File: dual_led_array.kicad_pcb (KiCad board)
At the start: 2 copper layers, 254 x 254 mm, 187 parts, among them J1 Screw_Terminal_01x02, J2 Screw_Terminal_01x02, M1 quarter_twenty, M2 quarter_twenty, M3 quarter_twenty, M4 quarter_twenty

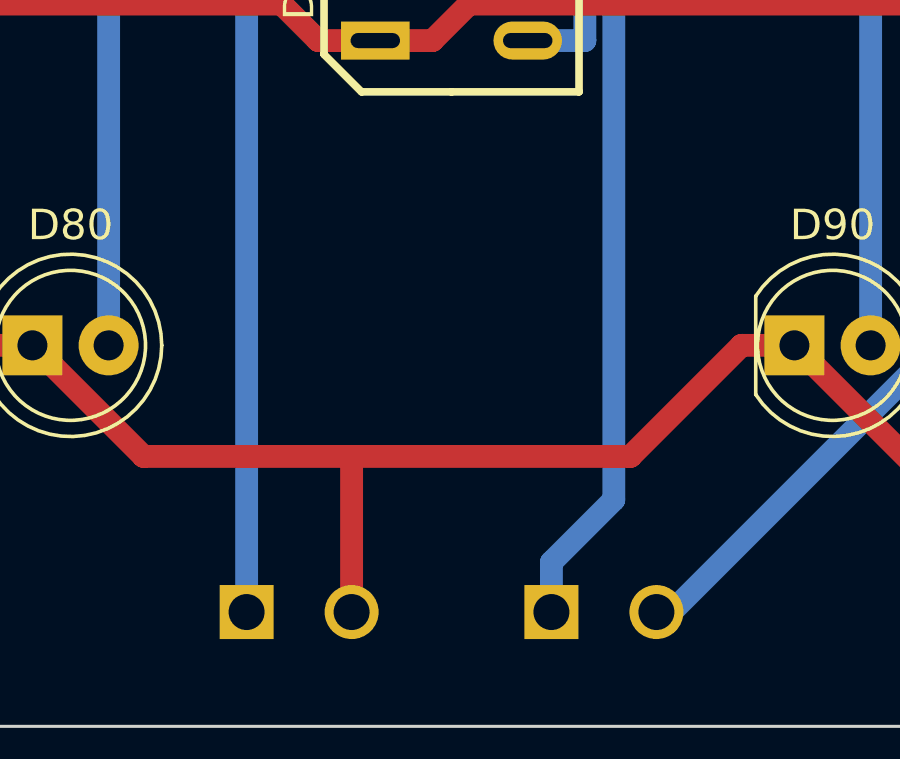
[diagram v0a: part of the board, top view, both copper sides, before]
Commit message: Added annotations to PCB.
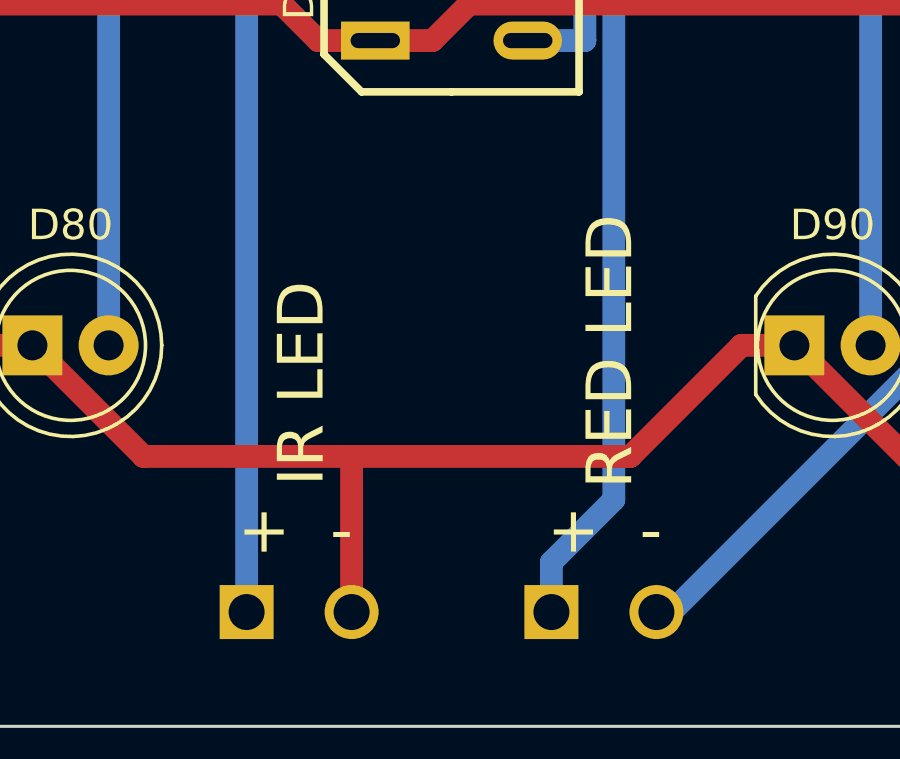
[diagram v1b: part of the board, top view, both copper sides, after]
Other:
- board text added: "+ -"
- board text added: "- +"
- board text added: "Dual LED Array V0.1 Dickinson Lab 2019"
- board text added: "IR LED"
- board text added: "RED LED"
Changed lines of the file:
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@@
   (general
     (thickness 1.6)
-    (drawings 10)
+    (drawings 21)
     (tracks 1220)
     (zones 0)
@@
     (descr BLOCK_CONN_2X1)
     (tags BLOCK_CONN_2X1)
-    (fp_text reference J1 (at -5.08 2.54) (layer B.SilkS)
+    (fp_text reference J1 (at -5.334 -2.7432) (layer B.SilkS)
       (effects (font (size 1.016 1.016) (thickness 0.2032)) (justify mirror))
     )
@@
     (descr BLOCK_CONN_2X1)
     (tags BLOCK_CONN_2X1)
-    (fp_text reference J2 (at -5.08 2.54) (layer B.SilkS)
+    (fp_text reference J2 (at 5.334 -2.8702) (layer B.SilkS)
       (effects (font (size 1.016 1.016) (thickness 0.2032)) (justify mirror))
     )
@@
       (net 94 "Net-(D101-Pad2)"))
   )
+  (gr_text "Dual LED Array V0.1\nDickinson Lab 2019" (at 177.8 300.5074) (layer B.SilkS)
+    (effects (font (size 1.524 1.524) (thickness 0.3048)) (justify mirror))
+  )
+  (gr_text "-  +" (at 259.1308 295.8338) (layer B.SilkS)
+    (effects (font (size 1.524 1.524) (thickness 0.3048)) (justify mirror))
+  )
+  (gr_text "-  +" (at 248.6914 295.8338) (layer B.SilkS)
+    (effects (font (size 1.524 1.524) (thickness 0.3048)) (justify mirror))
+  )
+  (gr_text "RED LED" (at 259.2324 290.4744 90) (layer B.SilkS)
+    (effects (font (size 1.524 1.524) (thickness 0.3048)) (justify mirror))
+  )
+  (gr_text "IR LED" (at 248.9454 291.2618 90) (layer B.SilkS)
+    (effects (font (size 1.524 1.524) (thickness 0.3048)) (justify mirror))
+  )
+  (gr_text "+  -" (at 259.1054 298.2722) (layer F.SilkS)
+    (effects (font (size 1.524 1.524) (thickness 0.3048)))
+  )
+  (gr_text "+  -" (at 248.793 298.2722) (layer F.SilkS)
+    (effects (font (size 1.524 1.524) (thickness 0.3048)))
+  )
+  (gr_text "RED LED" (at 259.2832 292.3032 90) (layer F.SilkS)
+    (effects (font (size 1.524 1.524) (thickness 0.3048)))
+  )
+  (gr_text "IR LED" (at 248.9962 293.37 90) (layer F.SilkS)
+    (effects (font (size 1.524 1.524) (thickness 0.3048)))
+  )
+  (dimension 254 (width 0.15) (layer Dwgs.User)
+    (gr_text "10.0000 in" (at 177.8 317.834799) (layer Dwgs.User)
+      (effects (font (size 1 1) (thickness 0.15)))
+    )
+    (feature1 (pts (xy 304.8 302.26) (xy 304.8 317.12122)))
+    (feature2 (pts (xy 50.8 302.26) (xy 50.8 317.12122)))
+    (crossbar (pts (xy 50.8 316.534799) (xy 304.8 316.534799)))
+    (arrow1a (pts (xy 304.8 316.534799) (xy 303.673496 317.12122)))
+    (arrow1b (pts (xy 304.8 316.534799) (xy 303.673496 315.948378)))
+    (arrow2a (pts (xy 50.8 316.534799) (xy 51.926504 317.12122)))
+    (arrow2b (pts (xy 50.8 316.534799) (xy 51.926504 315.948378)))
+  )
+  (dimension 254 (width 0.15) (layer Dwgs.User)
+    (gr_text "10.0000 in" (at 31.516801 177.8 270) (layer Dwgs.User)
+      (effects (font (size 1 1) (thickness 0.15)))
+    )
+    (feature1 (pts (xy 53.34 304.8) (xy 32.23038 304.8)))
+    (feature2 (pts (xy 53.34 50.8) (xy 32.23038 50.8)))
+    (crossbar (pts (xy 32.816801 50.8) (xy 32.816801 304.8)))
+    (arrow1a (pts (xy 32.816801 304.8) (xy 32.23038 303.673496)))
+    (arrow1b (pts (xy 32.816801 304.8) (xy 33.403222 303.673496)))
+    (arrow2a (pts (xy 32.816801 50.8) (xy 32.23038 51.926504)))
+    (arrow2b (pts (xy 32.816801 50.8) (xy 33.403222 51.926504)))
+  )
   (dimension 203.2 (width 0.15) (layer Dwgs.User)
